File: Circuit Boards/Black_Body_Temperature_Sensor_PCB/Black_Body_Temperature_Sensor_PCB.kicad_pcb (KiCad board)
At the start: 6 copper layers, 60 x 75.2 mm, 189 parts, among them J401 Screw_Terminal_01x02, J402 Screw_Terminal_01x02, J601 Conn_01x02_Pin, J701 Conn_01x06_Pin, J702 5040500891, J703 USB_C_Receptacle_USB2.0_16P, J704 Conn_01x04_Pin, P601 436500200, P701 pogo programmer, Q201 TMUX1112PWR, Q202 TMUX1112PWR, Q301 TMUX1112PWR, Q401 TMUX1112PWR, Q402 TMUX1112PWR, Q403 TMUX1112PWR, SW701 SW_MEC_5E, SW702 SW_MEC_5E, U201 LM334M, U301 LM334M, U302 LT1008, U501 OPA376xxDBV, U502 OPA376xxDBV, U503 OPA376xxDBV, U504 OPA376xxDBV, U505 AD8421ARZ, U506 AD8421ARZ, U507 ADS131M04xPW, U508 ISO7762FDBQ, U509 OPA376xxDBV, U601 LTC3260xMSE, U602 LT3094xMSE, U603 LT3042xMSE, U701 TXU0304, U702 ABM8G-25.000MHZ-18-D2Y-T, U703 USBLC6-2SC6, U704 STM32G431RBTx, U705 AMS1117-3.3

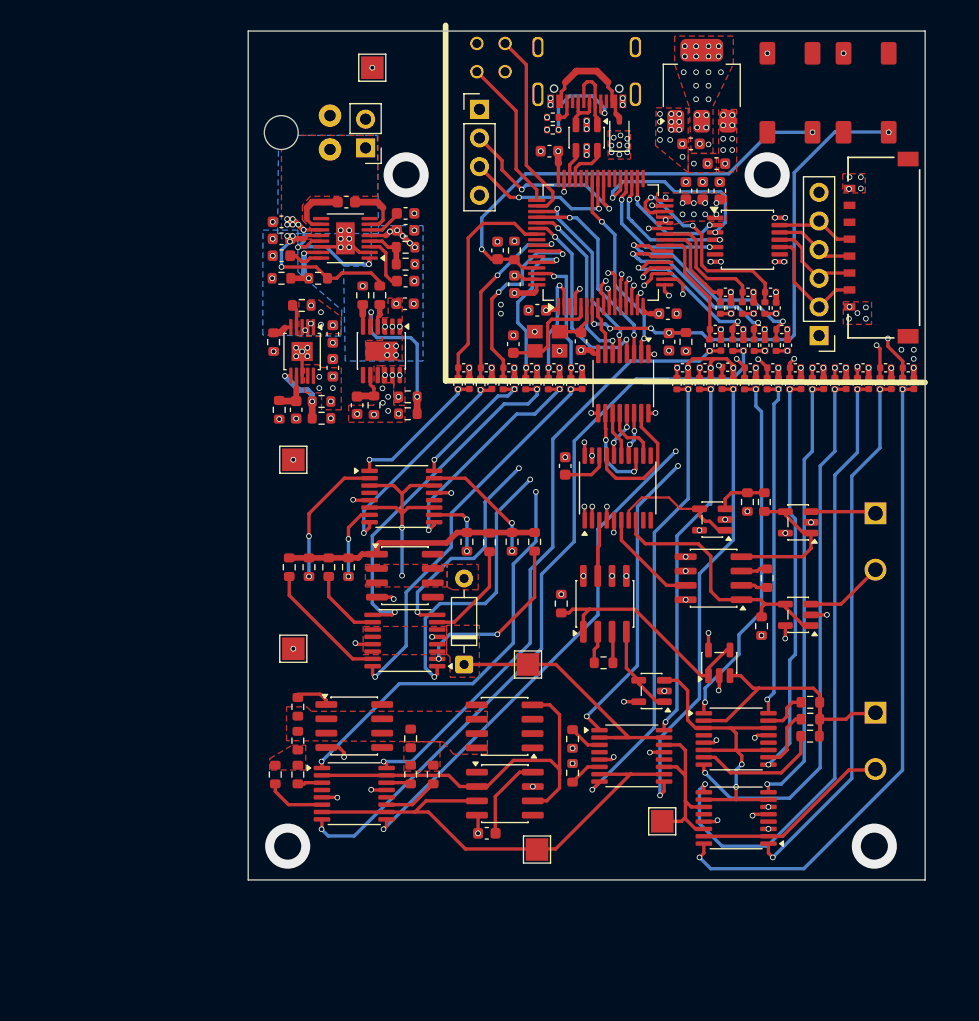
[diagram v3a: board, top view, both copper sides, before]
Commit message: Temp probe bom done
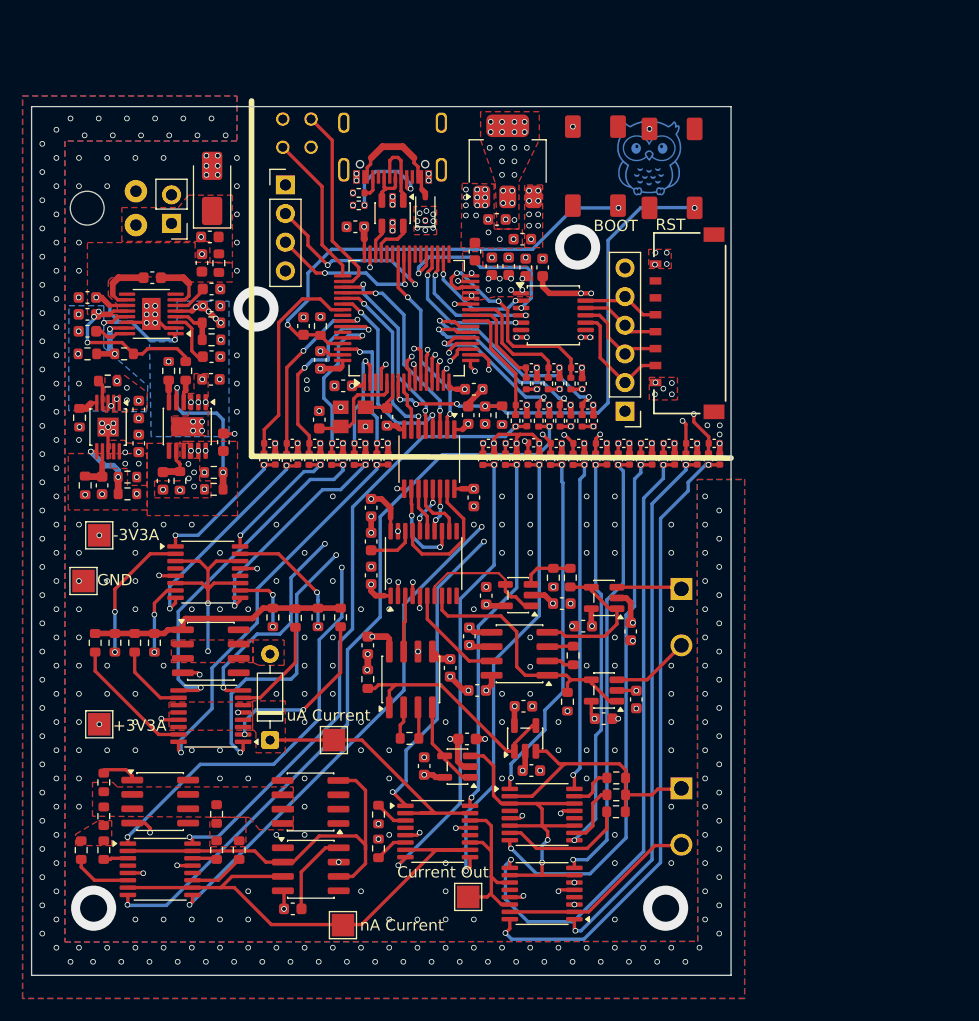
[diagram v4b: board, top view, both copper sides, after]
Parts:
- removed R705: 10k, Resistor_SMD:R_0603_1608Metric
- added C502: 0.1uf, Capacitor_SMD:C_0603_1608Metric, F.Cu at (206.5, 107.2)
- added C503: 0.1uf, Capacitor_SMD:C_0603_1608Metric, F.Cu at (204.7, 99.0)
- added C504: 0.1uf, Capacitor_SMD:C_0603_1608Metric, F.Cu at (199.4, 106.1)
- added C505: 0.1uf, Capacitor_SMD:C_0603_1608Metric, F.Cu at (190.6, 111.4)
- added C506: 0.1uf, Capacitor_SMD:C_0603_1608Metric, F.Cu at (196.1, 96.3)
- added C507: 0.1uf, Capacitor_SMD:C_0603_1608Metric, F.Cu at (185.6, 100.7)
- added C508: 0.1uf, Capacitor_SMD:C_0603_1608Metric, F.Cu at (192.9, 102.7)
- added C509: 0.1uf, Capacitor_SMD:C_0603_1608Metric, F.Cu at (194.6, 99.9)
- added C510: 0.1uf, Capacitor_SMD:C_0603_1608Metric, F.Cu at (195.3, 104.7)
- added C511: 0.1uf, Capacitor_SMD:C_0603_1608Metric, F.Cu at (185.9, 88.5)
- added C512: 0.1uf, Capacitor_SMD:C_0603_1608Metric, F.Cu at (185.9, 94.5)
- added C513: 0.1uf, Capacitor_SMD:C_0603_1608Metric, F.Cu at (195.0, 87.6)
- added C514: 0.1uf, Capacitor_SMD:C_0603_1608Metric, F.Cu at (194.5, 80.3)
- added C515: 0.1uf, Capacitor_SMD:C_0603_1608Metric, F.Cu at (209.4, 105.5)
- added C516: 0.1uf, Capacitor_SMD:C_0603_1608Metric, F.Cu at (208.9, 99.5)
- added C517: 0.1uf, Capacitor_SMD:C_0603_1608Metric, F.Cu at (200.1, 111.8)
- added C518: 0.1uf, Capacitor_SMD:C_0603_1608Metric, F.Cu at (194.4, 109.0)
- added C519: 0.1uf, Capacitor_SMD:C_0603_1608Metric, F.Cu at (202.8, 97.0)
- added C613: 4.7uf, Capacitor_SMD:C_0603_1608Metric, F.Cu at (172.8, 82.7)
- added C614: 10uf, Capacitor_SMD:C_0603_1608Metric, F.Cu at (171.6, 64.5)
- added C615: 10uf, Capacitor_SMD:C_0603_1608Metric, F.Cu at (170.9, 66.8)
- added C709: 0.1uf, Capacitor_SMD:C_0603_1608Metric, F.Cu at (199.6, 67.2)
- added C710: 0.1uf, Capacitor_SMD:C_0603_1608Metric, F.Cu at (201.1, 67.2)
- added D601: SMAJ24A, Diode_SMD:D_SMA, F.Cu at (171.8, 60.2)
- added G***: LOGO, LOGO, B.Cu at (210.5, 57.5)
- added R616: 500, Resistor_SMD:R_0603_1608Metric, F.Cu at (172.4, 66.8)
- added R703: 10k, Resistor_SMD:R_0603_1608Metric, F.Cu at (181.4, 72.4)
- R209: value 134 -> 133
- R210, R211: value 1.34k -> 1.33k
- R212, R213: value 13.4k -> 13.3k
- R216: value 1.34M -> 1.33M
- R405: value 5 -> 4.99
- R407: value 35k -> 33.2k
- R601, R604: value 570k -> 569k
- R606: value 499 -> 500
- R607, R609: value 200k -> 180k
- R611: value 453k -> 448k
- R612: value 49.9k -> 50k
- R613: value 450k -> 448k
- moved TP603 52.2 mm to (160.4, 95.0)
- moved C706 22.4 mm to (195.1, 65.8)
- moved SW702 18.9 mm to (207.8, 61.7), turned to 90 degrees
- moved R501 18.5 mm to (203.8, 101.6)
- moved C201 18.5 mm to (177.4, 84.2)
- moved C202 18.5 mm to (181.4, 84.2)
- moved C203 18.5 mm to (185.4, 84.2)
- moved C204 18.5 mm to (179.4, 84.2)
- moved C205 18.5 mm to (202.6, 77.5)
- moved C206 18.5 mm to (187.4, 84.2)
- moved C207 18.5 mm to (183.4, 84.2)
- moved C208 18.5 mm to (200.6, 77.5)
- moved C209 18.5 mm to (176.9, 82.8)
- moved C210 18.5 mm to (180.9, 82.8)
- moved C211 18.5 mm to (184.9, 82.8)
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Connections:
- J601 pad 1: 12Vin -> /power_supply/vin
- P601 pad 1: 12Vin -> /power_supply/vin
- SW702 pad 2: /micrcontroller/BOOT0 -> +3V3
- SW702 pad 3: GNDPWR -> /micrcontroller/BOOT0
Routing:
- net -3V3A: track 4.42 -> 19.1 mm
- net +3V3A: track 10.8 -> 25.4 mm
- net GND: track 11.5 -> 21.3 mm, vias 50 -> 355
- net /nA_current/nA_I_Source: track 43.2 -> 48.9 mm
- net 5Vin: track 0.00 -> 4.57 mm
- net GNDPWR: track 201.2 -> 197.7 mm, vias 83 -> 84
- net 12Vin: track 14.6 -> 17.5 mm, vias 8 -> 3
- net +3V3: track 161.7 -> 159.3 mm
- net /sensor_interface/selh2: track 58.2 -> 56.3 mm
- net /micrcontroller/sel_v.10uA: track 19.8 -> 19.1 mm
- net /nA_current/sel2: track 55.1 -> 55.8 mm
- net /uA_current/selt4: track 46.7 -> 47.5 mm
- net /uA_current/selt1: track 54.5 -> 55.3 mm
- net /micrcontroller/i_sense_sel1: track 21.7 -> 21.2 mm
- net +5VA: vias 10 -> 9
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- added copper zone on F.Cu, net /power_supply/vin
- added copper zone on B.Cu, net GND
- added copper zone on In2.Cu, net GND
- added copper zone on In3.Cu, net GND
- removed copper zone on B.Cu, net 12Vin
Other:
- board size 60 x 75.2 mm -> 62 x 77 mm
- board text added: "+3V3A"
- board text added: "-3V3A"
- board text added: "12V PWR IN"
- board text added: "3.3V SCL SDA GND"
- board text added: "5V CS MOSI CLK MISO GND"
- board text added: "5V NC NC CS MOSI CLK MISO GND"
- board text added: "BOOT"
- board text added: "Current Out"
- board text added: "DIGITAL ANALOG"
- board text added: "GND"
- board text added: "GND 12v"
- board text added: "I+ I-"
- board text added: "RST"
- board text added: "TEMPERATURE PROBE"
- board text added: "V+ V-"
- board text added: "nA Current"
- board text added: "uA Current"

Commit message: Designs finished - order placed
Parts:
- added D702: RED, LED_SMD:LED_0603_1608Metric, F.Cu at (181.0, 59.7)
- added R705: 1.33k, Resistor_SMD:R_0603_1608Metric, F.Cu at (181.0, 62.7)
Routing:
- net /micrcontroller/swdio: track 13.6 -> 15.0 mm
- net Net-(D702-A): track 0.00 -> 1.39 mm
- net GNDPWR: vias 84 -> 85
- net +3V3: vias 51 -> 52
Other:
- board text added: "TEMPERATURE SENSOR REV. 0"
